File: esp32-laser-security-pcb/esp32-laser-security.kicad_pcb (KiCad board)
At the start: 2 copper layers, 46.5 x 37.5 mm, 9 parts, among them J1 Conn_01x06, SW1 SW_Push

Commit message: added mount & updated pcb
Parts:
- added 220_ohm1: R, Resistor_THT:R_Axial_DIN0207_L6.3mm_D2.5mm_P7.62mm_Horizontal, F.Cu at (100.0, 80.5)
- added LED1: LED, LED_THT:LED_D5.0mm, F.Cu at (98.5, 73.0)
- added REF**: MountingHole_3.2mm_M3, MountingHole:MountingHole_3.2mm_M3, F.Cu at (117.0, 100.0)
- added REF**: MountingHole_3.2mm_M3, MountingHole:MountingHole_3.2mm_M3, F.Cu at (98.0, 100.0)
- moved REF** 14.5 mm to (126.5, 109.0)
- moved REF** 14.5 mm to (88.0, 109.0)
- moved R1 10.9 mm to (105.8, 100.1)
- moved 10k_ohm1 6.02 mm to (100.0, 86.0)
- moved BZ1 3.16 mm to (121.8, 83.5)
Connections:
- J1 pad 2: unconnected-(J1-Pin_2-Pad2) -> Net-(BZ1--)
- J1 pad 3: Net-(BZ1--) -> Net-(J1-Pin_3)
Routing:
- net Net-(LED1-A): track 0.00 -> 56.1 mm
- net Net-(J1-Pin_1): track 11.6 -> 47.5 mm
- net Net-(J1-Pin_3): track 0.00 -> 33.4 mm
- net Net-(J1-Pin_6): track 68.3 -> 54.4 mm
- net Net-(BZ1--): track 60.6 -> 73.3 mm
- net Net-(J1-Pin_5): track 42.1 -> 34.8 mm
- net Net-(BZ1-+): track 47.7 -> 54.3 mm
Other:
- board size 46.5 x 37.5 mm -> 46.5 x 52 mm
- board text added: "D2"
- board text removed: "5V"

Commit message: updated pcb
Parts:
- removed BZ1: Buzzer, Buzzer_Beeper:Buzzer_12x9.5RM7.6
- removed LED1: LED, LED_THT:LED_D5.0mm
- added 220_ohm2: R, Resistor_THT:R_Axial_DIN0207_L6.3mm_D2.5mm_P7.62mm_Horizontal, F.Cu at (97.4, 83.5)
- added 330_ohm1: R, Resistor_THT:R_Axial_DIN0207_L6.3mm_D2.5mm_P7.62mm_Horizontal, F.Cu at (119.6, 82.9)
- added 330_ohm2: R, Resistor_THT:R_Axial_DIN0207_L6.3mm_D2.5mm_P7.62mm_Horizontal, F.Cu at (126.9, 90.5)
- added D1: LED_Dual_AAK, LED_THT:LED_D5.0mm-3, F.Cu at (95.9, 75.0)
- added J2: LED_connector, Connector_JST:JST_XH_B3B-XH-AM_1x03_P2.50mm_Vertical, F.Cu at (108.5, 74.0)
- added J3: Conn_01x02_Pin, TerminalBlock:TerminalBlock_MaiXu_MX126-5.0-02P_1x02_P5.00mm, F.Cu at (138.7, 88.5)
- J1: value Conn_01x06 -> Conn_01x07; footprint Connector_PinHeader_2.54mm:PinHeader_1x06_P2.54mm_Vertical -> Connector_PinHeader_2.54mm:PinHeader_1x07_P2.54mm_Vertical
- moved REF** 15.0 mm to (141.5, 109.0)
- moved REF** 15.0 mm to (141.5, 65.0)
- moved 220_ohm1 11.7 mm to (111.4, 83.0), turned to -90 degrees
- moved RESET 11.5 mm to (125.5, 72.5)
- moved J1 7.94 mm to (90.0, 79.0), turned to 0 degrees
- moved LDR 7.10 mm to (112.2, 103.1)
- moved REF** 7.10 mm to (123.4, 103.0)
- moved REF** 7.10 mm to (104.4, 103.0)
- moved 10k_ohm1 4.78 mm to (97.4, 90.0)
- moved REF** 2.00 mm to (86.0, 65.0)
- moved REF** 2.00 mm to (86.0, 109.0)
- renumbered R1 to LDR, SW1 to RESET
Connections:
- 10k_ohm1 pad 1: Net-(BZ1--) -> /GND
- 10k_ohm1 pad 2: Net-(J1-Pin_6) -> /D34
- 220_ohm1 pad 1: Net-(J1-Pin_3) -> Net-(J2-Pin_2)
- 220_ohm1 pad 2: Net-(LED1-A) -> /D4
- J1 pad 1: Net-(J1-Pin_1) -> /D34
- J1 pad 2: Net-(BZ1--) -> /D18
- J1 pad 3: Net-(J1-Pin_3) -> /D5
- J1 pad 4: Net-(BZ1-+) -> /D4
- J1 pad 5: Net-(J1-Pin_5) -> /D2
- J1 pad 6: Net-(J1-Pin_6) -> /GND
- LDR pad 1: Net-(J1-Pin_1) -> /3V3
- LDR pad 2: Net-(J1-Pin_6) -> /D34
- RESET pad 1: Net-(J1-Pin_5) -> /D18
- RESET pad 2: Net-(BZ1--) -> /GND
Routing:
- net /GND: track 0.00 -> 106.6 mm
- net Net-(BZ1--): track 73.3 -> 0.00 mm
- net /D34: track 0.00 -> 71.1 mm
- net /D5: track 0.00 -> 70.7 mm
- net Net-(D1-A1): track 0.00 -> 59.4 mm
- net /D2: track 0.00 -> 56.7 mm
- net Net-(LED1-A): track 56.1 -> 0.00 mm
- net /D18: track 0.00 -> 55.5 mm
- net Net-(J1-Pin_6): track 54.4 -> 0.00 mm
- net Net-(BZ1-+): track 54.3 -> 0.00 mm
- net Net-(J1-Pin_1): track 47.5 -> 0.00 mm
- net /D4: track 0.00 -> 36.4 mm
- net Net-(J1-Pin_5): track 34.8 -> 0.00 mm
- net Net-(J1-Pin_3): track 33.4 -> 0.00 mm
- net Net-(D1-A2): track 0.00 -> 32.0 mm
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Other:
- board size 46.5 x 52 mm -> 63.5 x 52 mm
- board text added: "+"
- board text added: "-"
- board text added: "BUZZ"
- board text added: "G"
- board text added: "GRN"
- board text added: "LDR"
- board text added: "R"
- board text added: "RED"
- board text added: "RST"
- board text removed: "D18"
- board text removed: "D2"
- board text removed: "D34"
- board text removed: "D5"

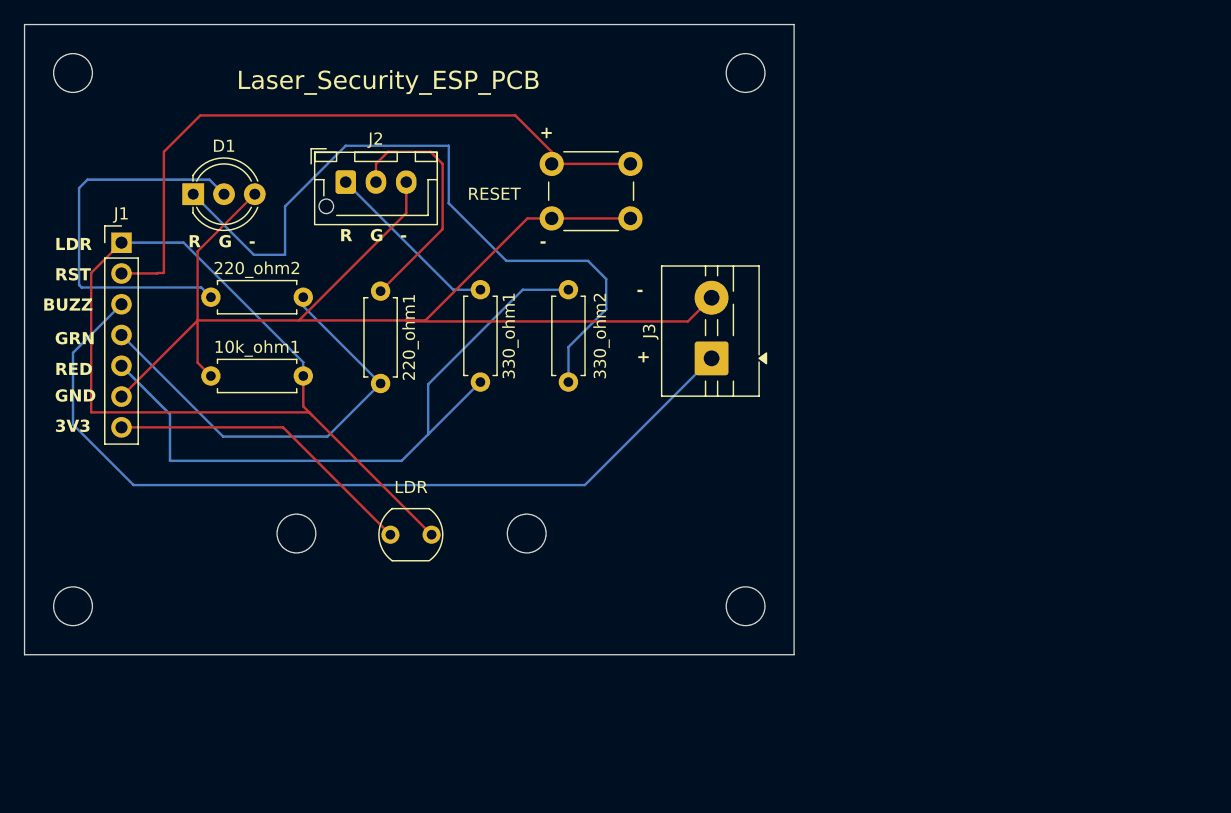
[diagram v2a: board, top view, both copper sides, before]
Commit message: updated pcb schematic and gerber files for industry
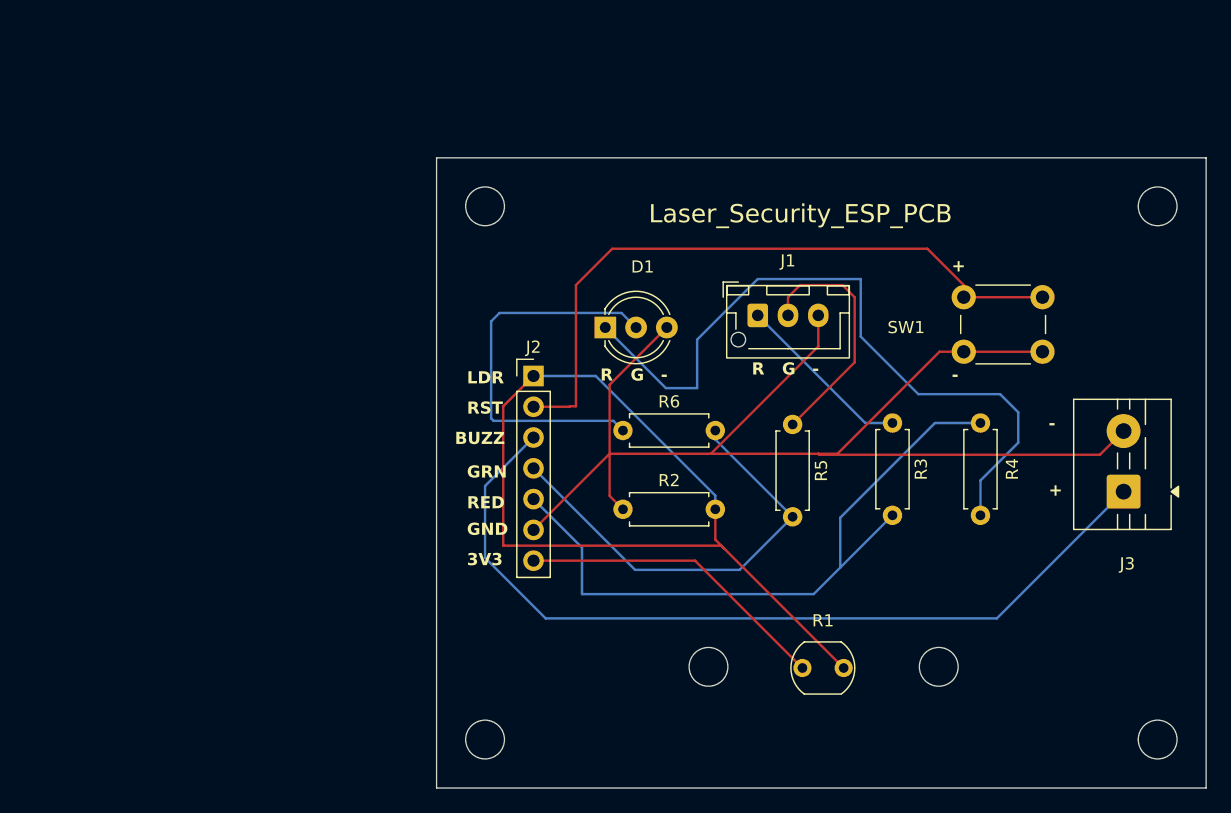
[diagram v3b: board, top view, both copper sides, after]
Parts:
- D1: value LED_Dual_AAK -> LED RG BIPOLAR
- J1: renamed from J2; value LED_connector -> EXT LED RG BIPOLAR
- J2: renamed from J1; value Conn_01x07 -> Headers
- J3: value Conn_01x02_Pin -> EXT BUZZER
- R1: renamed from LDR; value R_Photo -> LDR
- R2: renamed from 10k_ohm1; value R -> 10kΩ
- R3: renamed from 330_ohm1; value R -> 330Ω
- R4: renamed from 330_ohm2; value R -> 330Ω
- R5: renamed from 220_ohm1; value R -> 220Ω
- R6: renamed from 220_ohm2; value R -> 220Ω
- SW1: renamed from RESET; value SW_Push -> RESET BUTTON
- moved R1 35.7 mm to (146.2, 114.1)
- moved REF** 35.7 mm to (157.4, 114.0)
- moved REF** 35.7 mm to (138.4, 114.0)
- moved J1 35.7 mm to (142.5, 85.0)
- moved J2 35.7 mm to (124.0, 90.0)
- moved J3 35.7 mm to (172.7, 99.5)
- moved R2 35.7 mm to (131.4, 101.0)
- moved R3 35.7 mm to (153.6, 93.9)
- moved R4 35.7 mm to (160.9, 101.5)
- moved R5 35.7 mm to (145.4, 94.0)
- moved R6 35.7 mm to (131.4, 94.5)
- moved REF** 35.7 mm to (175.5, 120.0)
- moved REF** 35.7 mm to (175.5, 76.0)
- moved REF** 35.7 mm to (120.0, 76.0)
- moved REF** 35.7 mm to (120.0, 120.0)
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
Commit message: updated pcb schematic and gerber files for industry
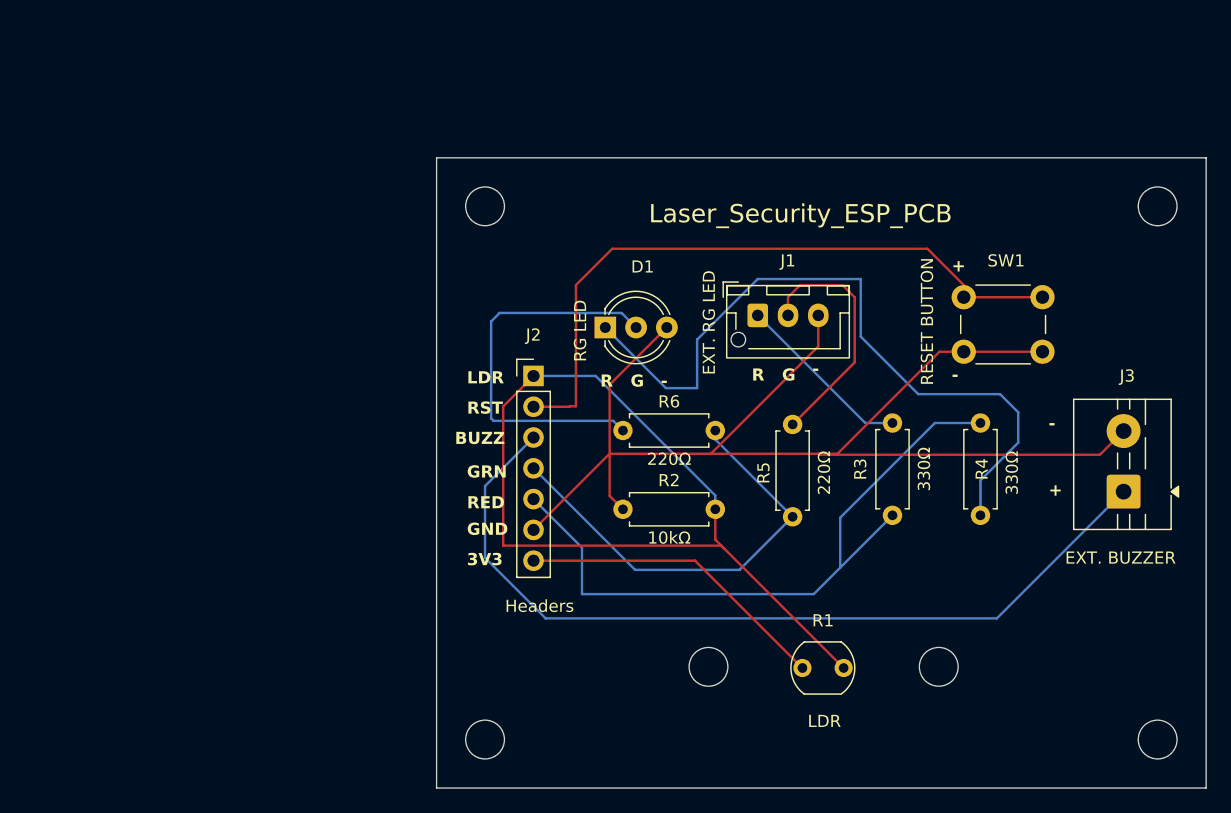
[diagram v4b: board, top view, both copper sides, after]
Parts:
- D1: value LED RG BIPOLAR -> RG LED
- J1: value EXT LED RG BIPOLAR -> EXT. RG LED
- J3: value EXT BUZZER -> EXT. BUZZER
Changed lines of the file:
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@@
 		(tags "Resistor Axial_DIN0207 series Axial Horizontal pin pitch 7.62mm 0.25W = 1/4W length 6.3mm diameter 2.5mm")
 		(property "Reference" "R4"
-			(at 3.81 2.63 90)
+			(at 3.81 0.13 90)
 			(layer "F.SilkS")
 			(effects
@@
 		)
 		(property "Value" "330Ω"
-			(at 3.81 2.37 90)
-			(layer "F.Fab")
+			(at 3.5 2.62 90)
+			(layer "F.SilkS")
 			(effects
 				(font
@@
 		)
 		(fp_text user "${REFERENCE}"
-			(at 3.81 0 90)
+			(at 3.81 -2.5 90)
 			(layer "F.Fab")
 			(effects
@@
 		(tags "Through hole pin header THT 1x07 2.54mm single row")
 		(property "Reference" "J2"
-			(at 0 -2.38 0)
+			(at 0 -3.38 0)
 			(layer "F.SilkS")
 			(effects
@@
 		)
 		(property "Value" "Headers"
-			(at 0 17.62 0)
-			(layer "F.Fab")
+			(at 0.5 19 0)
+			(layer "F.SilkS")
 			(effects
 				(font
@@
 		(property "Value" "10kΩ"
 			(at 3.81 2.37 0)
-			(layer "F.Fab")
+			(layer "F.SilkS")
 			(effects
 				(font
@@
 		(tags "Resistor Axial_DIN0207 series Axial Horizontal pin pitch 7.62mm 0.25W = 1/4W length 6.3mm diameter 2.5mm")
 		(property "Reference" "R5"
-			(at 3.81 -2.37 90)
+			(at 4 2.38 90)
 			(layer "F.SilkS")
 			(effects
@@
 		)
 		(property "Value" "220Ω"
-			(at 3.81 2.37 90)
-			(layer "F.Fab")
+			(at 4 -2.62 90)
+			(layer "F.SilkS")
 			(effects
 				(font
@@
 		)
 		(property "Value" "LDR"
-			(at 1.5 3 0)
-			(layer "F.Fab")
+			(at 1.810468 4.403811 0)
+			(layer "F.SilkS")
 			(effects
 				(font
@@
 		(tags "THT terminal block MaiXu MX126-5.0-02P pitch 5mm size 10.5x7.8mm drill 1.3mm pad 2.8mm")
 		(property "Reference" "J3"
-			(at -5.955553 0.308289 180)
+			(at 9.544447 0.308289 180)
 			(layer "F.SilkS")
 			(effects
@@
 			)
 		)
-		(property "Value" "EXT BUZZER"
-			(at 2.25 4.92 90)
-			(layer "F.Fab")
+		(property "Value" "EXT. BUZZER"
+			(at -5.476831 -0.256634 0)
+			(layer "F.SilkS")
 			(effects
 				(font
@@
 			)
 		)
-		(property "Value" "EXT LED RG BIPOLAR"
-			(at 2.5 4.6 0)
-			(layer "F.Fab")
+		(property "Value" "EXT. RG LED"
+			(at -4 0.6 90)
+			(layer "F.SilkS")
 			(effects
 				(font
@@
 		(tags "tact sw push 6mm")
 		(property "Reference" "SW1"
-			(at -4.75 2.5 0)
+			(at 3.5 -3 0)
 			(layer "F.SilkS")
 			(effects
@@
 		)
 		(property "Value" "RESET BUTTON"
-			(at 3.75 6.7 0)
-			(layer "F.Fab")
+			(at -3 2 90)
+			(layer "F.SilkS")
 			(effects
 				(font
@@
 		(property "Value" "220Ω"
 			(at 3.81 2.37 0)
-			(layer "F.Fab")
+			(layer "F.SilkS")
 			(effects
 				(font
@@
 		(tags "Resistor Axial_DIN0207 series Axial Horizontal pin pitch 7.62mm 0.25W = 1/4W length 6.3mm diameter 2.5mm")
 		(property "Reference" "R3"
-			(at 3.81 -2.37 90)
+			(at 3.81 2.63 90)
 			(layer "F.SilkS")
 			(effects
@@
 		)
 		(property "Value" "330Ω"
-			(at 3.81 2.37 90)
-			(layer "F.Fab")
+			(at 3.81 -2.63 90)
+			(layer "F.SilkS")
 			(effects
 				(font
@@
 			)
 		)
-		(property "Value" "LED RG BIPOLAR"
-			(at 2.54 3.96 0)
-			(layer "F.Fab")
+		(property "Value" "RG LED"
+			(at -2.043642 0.274334 90)
+			(layer "F.SilkS")
 			(effects
 				(font
@@
 	)
 	(gr_text "R"
-		(at 129.5 90.5 0)
+		(at 129.5 91 0)
 		(layer "F.SilkS")
 		(effects
@@
 	)
 	(gr_text "G"
-		(at 132 90.5 0)
+		(at 132 91 0)
 		(layer "F.SilkS")
 		(effects
@@
 	)
 	(gr_text "-"
-		(at 134.5 90.5 0)
+		(at 134.5 91 0)
 		(layer "F.SilkS")
 		(effects
@@
 	)
 	(gr_text "R"
-		(at 142 90 0)
+		(at 142 90.5 0)
 		(layer "F.SilkS")
 		(effects
@@
 	)
 	(gr_text "G"
-		(at 144.5 90 0)
+		(at 144.5 90.5 0)
 		(layer "F.SilkS")
 		(effects
@@
 	)
 	(segment
-		(start 120.700001 93.700001)
-		(end 120.5 93.5)
-		(width 0.2)
-		(layer "B.Cu")
-		(net "Net-(D1-A2)")
-	)
-	(segment
-		(start 130.580001 93.700001)
-		(end 120.700001 93.700001)
+		(start 150.5 88.88)
+		(end 145.38 94)
 		(width 0.2)
-		(layer "B.Cu")
-		(net "Net-(D1-A2)")
+		(layer "F.Cu")
+		(net "Net-(J1-Pin_2)")
 	)
 	(segment
-		(start 120.5 93.5)
-		(end 120.5 85.5)
+		(start 149.5 82.5)
+		(end 150.5 83.5)
 		(width 0.2)
-		(layer "B.Cu")
-		(net "Net-(D1-A2)")
+		(layer "F.Cu")
+		(net "Net-(J1-Pin_2)")
 	)
 	(segment
-		(start 131.38 94.5)
-		(end 130.580001 93.700001)
+		(start 150.5 83.5)
+		(end 150.5 88.88)
 		(width 0.2)
-		(layer "B.Cu")
-		(net "Net-(D1-A2)")
+		(layer "F.Cu")
+		(net "Net-(J1-Pin_2)")
 	)
 	(segment
-		(start 120.5 85.5)
-		(end 121.2 84.8)
+		(start 145 83.5)
+		(end 146 82.5)
 		(width 0.2)
-		(layer "B.Cu")
-		(net "Net-(D1-A2)")
+		(layer "F.Cu")
+		(net "Net-(J1-Pin_2)")
 	)
 	(segment
-		(start 121.2 84.8)
-		(end 131.26 84.8)
+		(start 146 82.5)
+		(end 149.5 82.5)
 		(width 0.2)
-		(layer "B.Cu")
-		(net "Net-(D1-A2)")
+		(layer "F.Cu")
+		(net "Net-(J1-Pin_2)")
 	)
 	(segment
-		(start 131.26 84.8)
-		(end 132.46 86)
+		(start 145 85)
+		(end 145 83.5)
 		(width 0.2)
-		(layer "B.Cu")
-		(net "Net-(D1-A2)")
+		(layer "F.Cu")
+		(net "Net-(J1-Pin_2)")
 	)
 	(segment
@@
 	)
 	(segment
-		(start 150.5 88.88)
-		(end 145.38 94)
+		(start 120.700001 93.700001)
+		(end 120.5 93.5)
 		(width 0.2)
-		(layer "F.Cu")
-		(net "Net-(J1-Pin_2)")
+		(layer "B.Cu")
+		(net "Net-(D1-A2)")
 	)
 	(segment
-		(start 149.5 82.5)
-		(end 150.5 83.5)
+		(start 130.580001 93.700001)
+		(end 120.700001 93.700001)
 		(width 0.2)
-		(layer "F.Cu")
-		(net "Net-(J1-Pin_2)")
+		(layer "B.Cu")
+		(net "Net-(D1-A2)")
 	)
 	(segment
-		(start 150.5 83.5)
-		(end 150.5 88.88)
+		(start 120.5 93.5)
+		(end 120.5 85.5)
 		(width 0.2)
-		(layer "F.Cu")
-		(net "Net-(J1-Pin_2)")
+		(layer "B.Cu")
+		(net "Net-(D1-A2)")
 	)
 	(segment
-		(start 145 83.5)
-		(end 146 82.5)
+		(start 131.38 94.5)
+		(end 130.580001 93.700001)
 		(width 0.2)
-		(layer "F.Cu")
-		(net "Net-(J1-Pin_2)")
+		(layer "B.Cu")
+		(net "Net-(D1-A2)")
 	)
 	(segment
-		(start 146 82.5)
-		(end 149.5 82.5)
+		(start 120.5 85.5)
+		(end 121.2 84.8)
 		(width 0.2)
-		(layer "F.Cu")
-		(net "Net-(J1-Pin_2)")
+		(layer "B.Cu")
+		(net "Net-(D1-A2)")
 	)
 	(segment
-		(start 145 85)
-		(end 145 83.5)
+		(start 121.2 84.8)
+		(end 131.26 84.8)
 		(width 0.2)
-		(layer "F.Cu")
-		(net "Net-(J1-Pin_2)")
+		(layer "B.Cu")
+		(net "Net-(D1-A2)")
+	)
+	(segment
+		(start 131.26 84.8)
+		(end 132.46 86)
+		(width 0.2)
+		(layer "B.Cu")
+		(net "Net-(D1-A2)")
 	)
 	(embedded_fonts no)
